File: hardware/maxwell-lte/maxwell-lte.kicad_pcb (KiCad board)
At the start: 2 copper layers, 69 x 41 mm, 23 parts, among them J1 LTE, J2 GPS, J3 Input, J4 SIM_Card, U1 MIC5209-ADJ, U2 SIM7000A, U3 TXB0104D, U4 SC16IS750IPW, Y1 Crystal

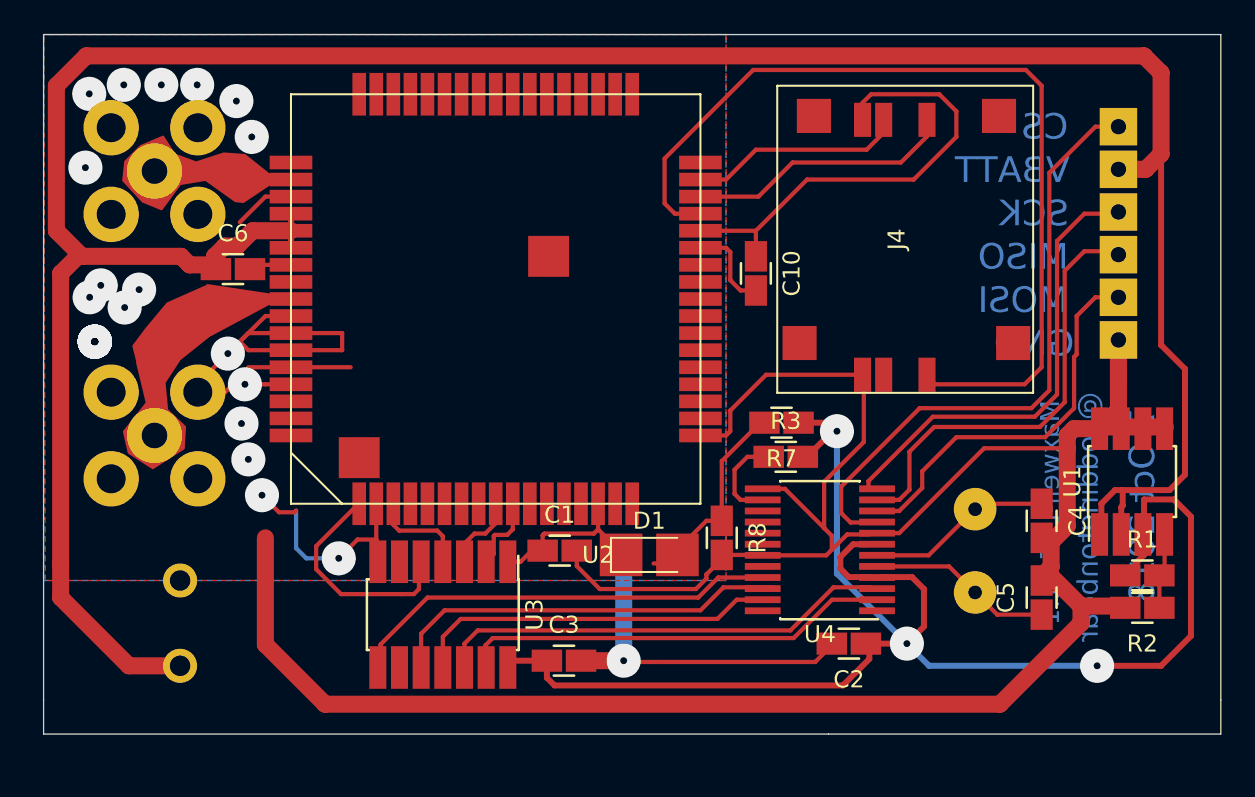
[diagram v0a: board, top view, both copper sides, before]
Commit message: Increasing minimum track width from 0.25 to 0.35 to make traces a little more resilient.
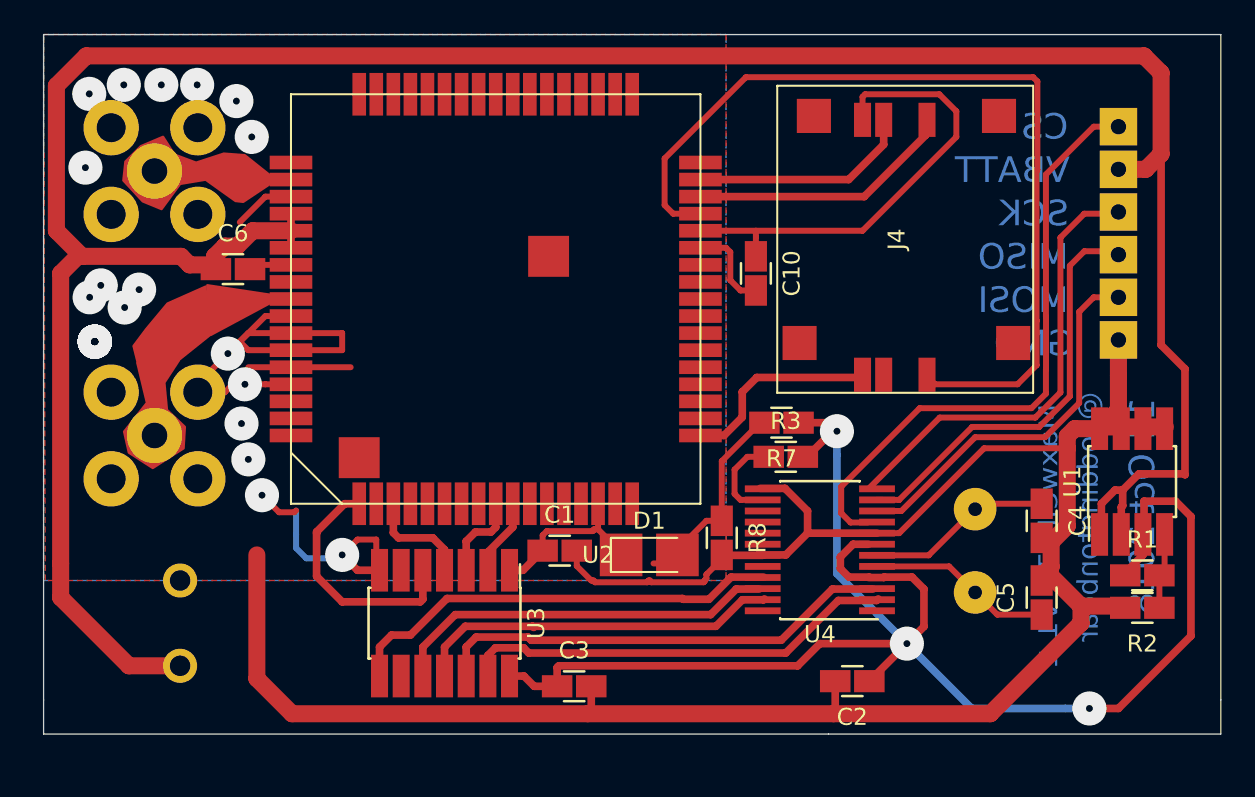
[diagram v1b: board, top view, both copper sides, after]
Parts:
- moved C2 2.21 mm to (135.4, 97.9)
- moved C3 1.62 mm to (119.1, 98.2)
- moved U3 0.51 mm to (111.5, 94.5)
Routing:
- net GND: track 227.2 -> 200.6 mm, vias 27 -> 26
- net +3V3: track 90.9 -> 95.2 mm
- net Net-(J4-Pad2): track 12.6 -> 14.0 mm
- net MISO: track 26.9 -> 25.6 mm
- net PWRKEY: track 13.8 -> 15.0 mm
- net Net-(U3-Pad13): track 24.6 -> 25.7 mm
- net /LTE_DO_L: track 4.60 -> 5.65 mm
- net Net-(U3-Pad12): track 26.2 -> 27.1 mm
- net EN_OUTPUT: track 25.1 -> 25.9 mm
- net /LTE_DTR_L: track 5.66 -> 6.42 mm
- net Net-(J4-Pad7): track 53.5 -> 52.7 mm
- net Net-(U3-Pad10): track 23.4 -> 22.8 mm
- net MOSI: track 23.8 -> 23.3 mm
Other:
- net class Default: clearance 0.2 -> 0.18; trace_width 0.25 -> 0.45
- net class Power: clearance 0.2 -> 0.18; trace_width 0.35 -> 0.45
- net class RF: clearance 0.2 -> 0.18
- rule solder_mask_min_width: 0.25 -> 0.35
- rule trace_clearance: 0.2 -> 0.18
- board text added: "14 Oct 2018"
- board text added: "Maxwell-LTE v1.2"
- board text removed: "7 Oct 2018"
- board text removed: "Maxwell-LTE v1.1"

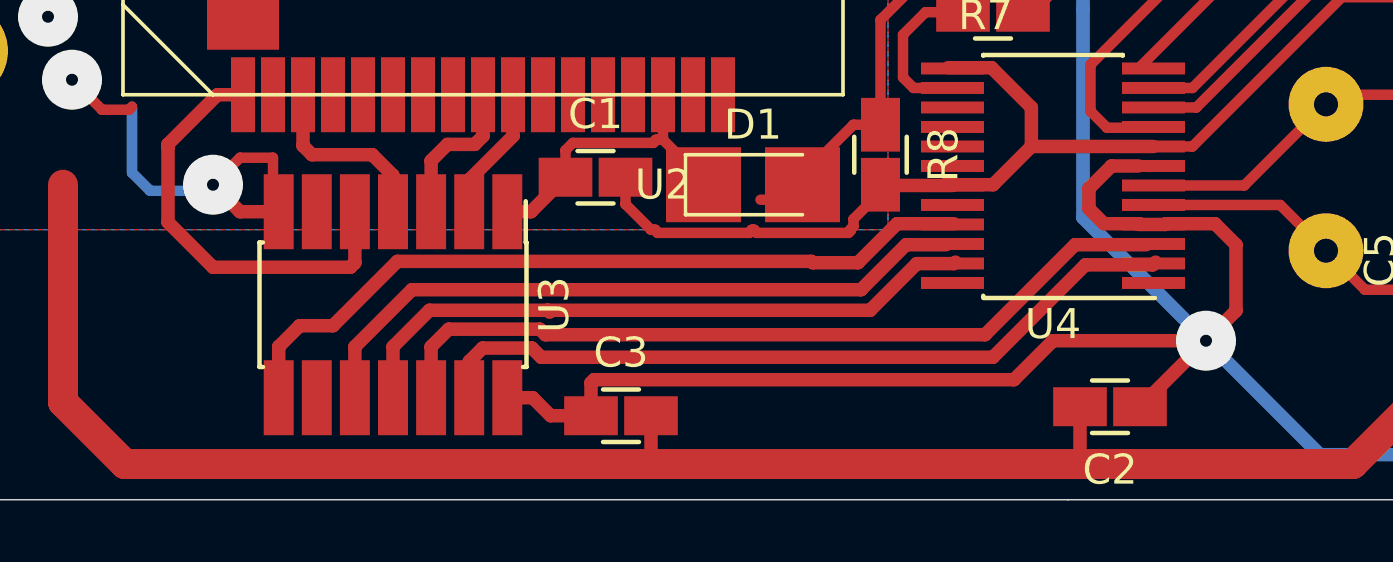
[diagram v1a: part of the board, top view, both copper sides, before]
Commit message: Give a direct link to PWRKEY from the level converter in case my bootstrapping strategy is unworkable.
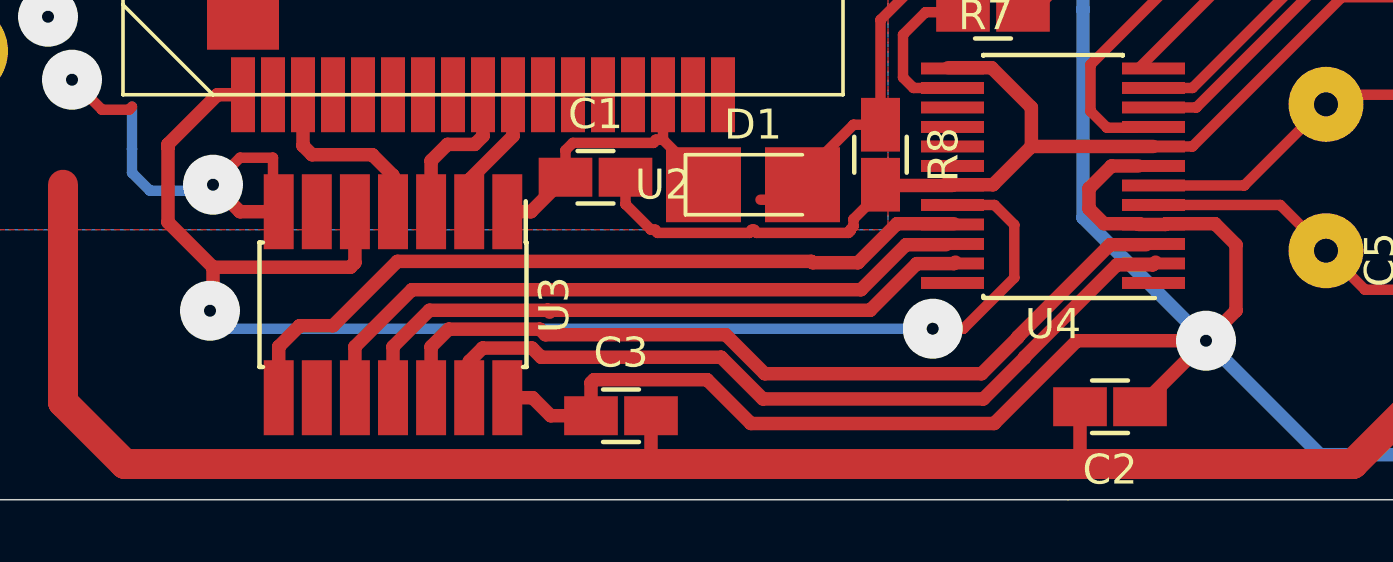
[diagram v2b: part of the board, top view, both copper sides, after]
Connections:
- U4 pad 20: (no net) -> PWRKEY
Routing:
- net PWRKEY: track 15.0 -> 48.4 mm, vias 0 -> 2
- net +3V3: track 95.2 -> 96.4 mm
- net Net-(U3-Pad13): track 25.7 -> 26.9 mm
- net Net-(U3-Pad12): track 27.1 -> 28.2 mm
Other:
- net class Default: trace_width 0.45 -> 0.35

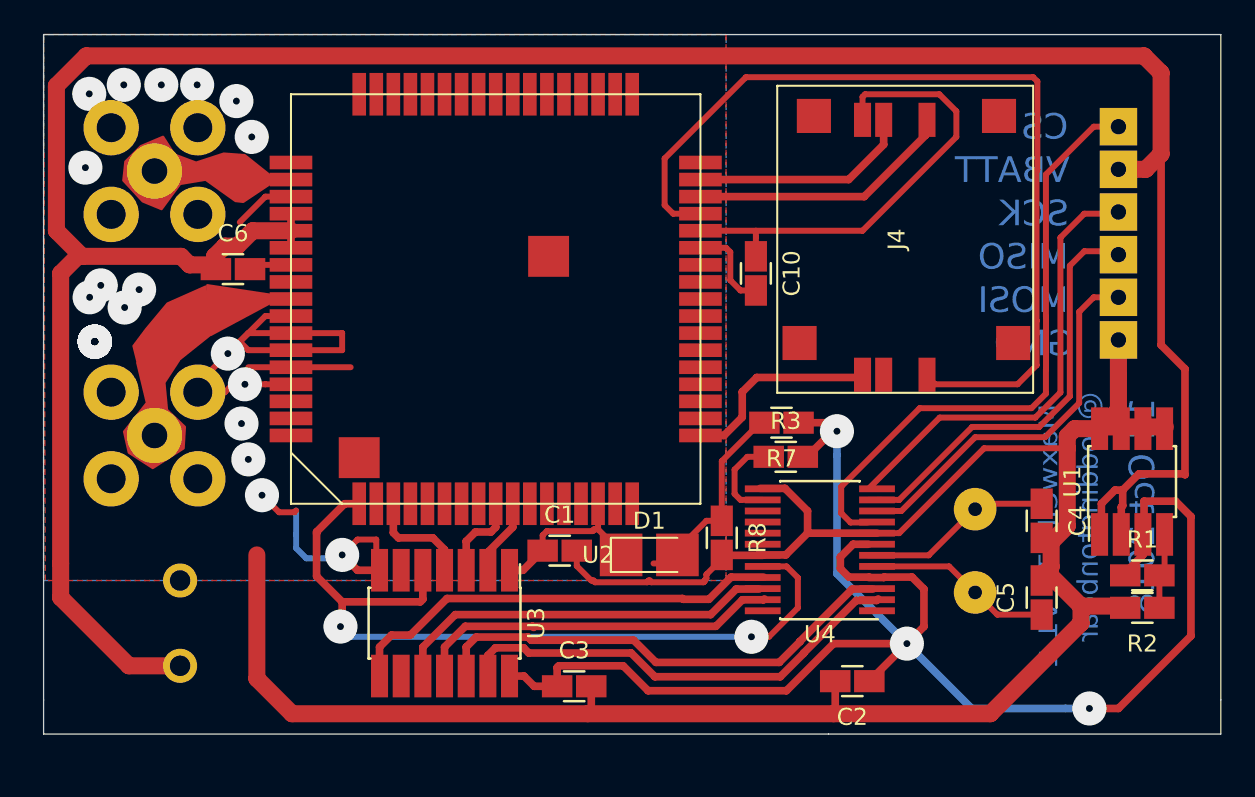
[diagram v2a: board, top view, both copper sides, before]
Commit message: Updating to v1.4; adds output capacitor to onboard regulator; adds status input to level shifter.
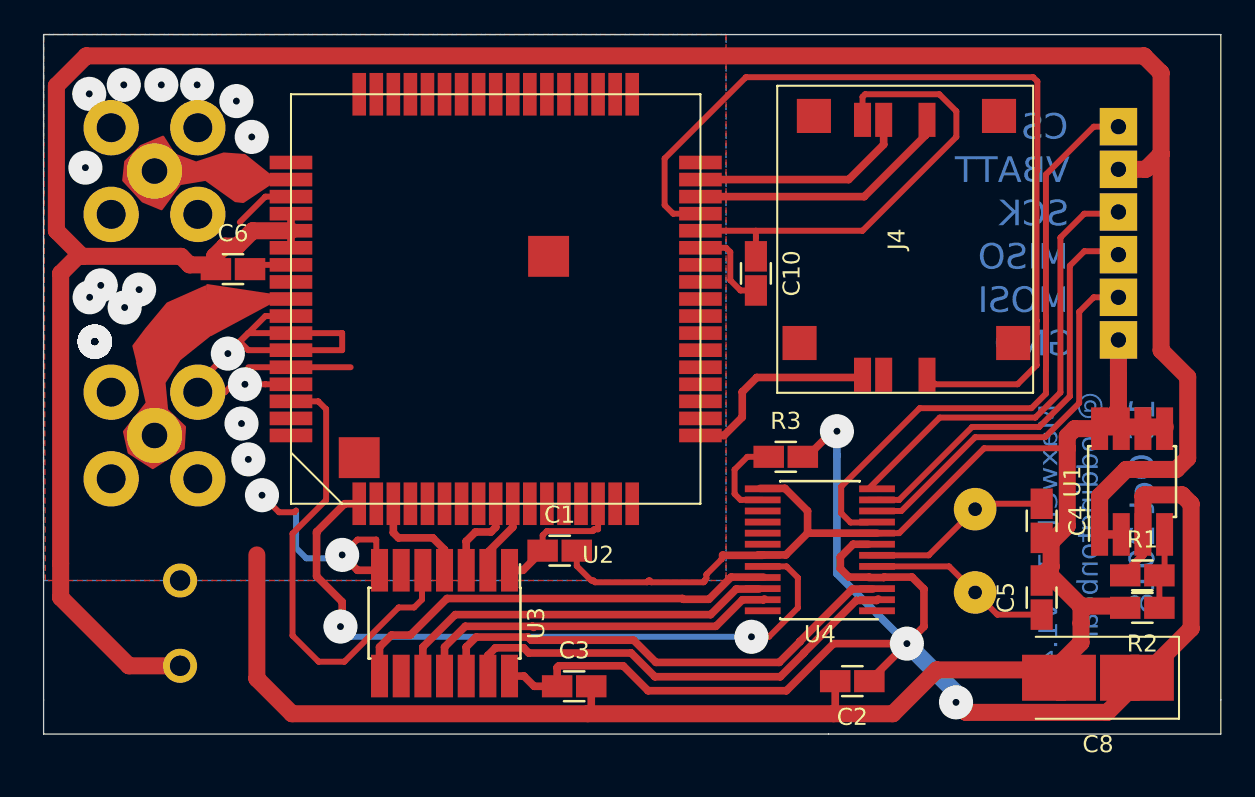
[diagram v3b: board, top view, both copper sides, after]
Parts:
- removed D1: 1N4148W, coddingtonbear:D_SOD-123_LargePads
- removed R7: 1k, coddingtonbear:0805_Milling
- removed R8: 3.6k, coddingtonbear:0805_Milling
- added C8: 100u / NTC-T107K10TRDF, coddingtonbear:CP_Tantalum_Case-D_EIA-7343-31_Milling, F.Cu at (149.8, 97.7)
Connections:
- U2 pad 66: (no net) -> STATUS
- U3 pad 5: PWRKEY -> STATUS
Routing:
- net STATUS: track 0.00 -> 28.3 mm
- net Net-(D1-Pad2): track 11.1 -> 0.00 mm
- net PWRKEY: track 48.4 -> 41.5 mm
- net GND: track 200.6 -> 205.1 mm
- net +1V8: track 10.4 -> 8.23 mm
- net +BATT: track 160.6 -> 159.0 mm
- net +3V3: track 96.4 -> 97.1 mm
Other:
- board text added: "16 Oct 2018"
- board text added: "Maxwell-LTE v1.4"
- board text removed: "14 Oct 2018"
- board text removed: "Maxwell-LTE v1.2"

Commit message: Finalizing v1.4.
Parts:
- added C11: 220u / TAJC227K006RNJ, coddingtonbear:CP_Tantalum_Case-C_EIA-6032-28_Milling, F.Cu at (95.9, 96.2)
- added C9: 220u / TAJC227K006RNJ, coddingtonbear:CP_Tantalum_Case-C_EIA-6032-28_Milling, F.Cu at (100.0, 96.2)
- added J10: Stitching, coddingtonbear:Thermal_Relief_Via_Milling, F.Cu at (100.2, 85.2)
- added J11: Stitching, coddingtonbear:Thermal_Relief_Via_Milling, F.Cu at (99.8, 82.3)
- added J12: Stitching, coddingtonbear:Thermal_Relief_Via_Milling, F.Cu at (91.7, 74.9)
- added J13: Stitching, coddingtonbear:Thermal_Relief_Via_Milling, F.Cu at (99.4, 78.7)
- added J14: Stiching, coddingtonbear:Thermal_Relief_Via_Milling, F.Cu at (90.9, 89.2)
- added J15: Stitching, coddingtonbear:Thermal_Relief_Via_Milling, F.Cu at (93.4, 89.3)
- added J16: Stitching, coddingtonbear:Thermal_Relief_Via_Milling, F.Cu at (96.3, 89.2)
- added J17: Stitching, coddingtonbear:Thermal_Relief_Via_Milling, F.Cu at (98.8, 88.9)
- added J18: Stitching, coddingtonbear:Thermal_Relief_Via_Milling, F.Cu at (101.2, 87.9)
- added J5: Stitching, coddingtonbear:Thermal_Relief_Via_Milling, F.Cu at (91.5, 77.4)
- added J6: Stitching, coddingtonbear:Thermal_Relief_Via_Milling, F.Cu at (94.3, 74.8)
- added J7: Stitching, coddingtonbear:Thermal_Relief_Via_Milling, F.Cu at (99.6, 63.1)
- added J8: Stitching, coddingtonbear:Thermal_Relief_Via_Milling, F.Cu at (100.5, 65.6)
- added J9: Stitching, coddingtonbear:Thermal_Relief_Via_Milling, F.Cu at (94.4, 63.1)
- added R4: 10k, coddingtonbear:0805_Milling, F.Cu at (124.2, 92.6)
- C7: value 0.1 / FG0H104ZF -> 220u / TAJC227K006RNJ; footprint Capacitor_THT:C_Disc_D11.0mm_W5.0mm_P5.00mm -> coddingtonbear:CP_Tantalum_Case-C_EIA-6032-28_Milling; moved to F.Cu
- moved C7 4.24 mm to (91.8, 96.2)
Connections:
- net Net-(U3-Pad10) renamed /STATUS_H
- net Net-(U3-Pad11) renamed /LTE_DTR_H
- net Net-(U3-Pad12) renamed /LTE_DO_H
- net Net-(U3-Pad13) renamed /LTE_DI_H
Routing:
- net GND: track 205.1 -> 219.9 mm, vias 26 -> 2
- net +BATT: track 159.0 -> 165.9 mm
- net /STATUS_H: track 22.8 -> 25.6 mm
- net STATUS: track 28.3 -> 26.7 mm
